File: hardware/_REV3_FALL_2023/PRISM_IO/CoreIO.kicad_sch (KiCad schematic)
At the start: 35 parts, among them J1 Conn_01x04_Socket, J2 COTS_SWITCH_PLUG, J3 PYRO 1, J4 PYRO 2, Q1 AO3400A, Q2 AO3400A, U1 TMC2209_SILENTSTEPSTICK, U2 LD1117S12TR_SOT223

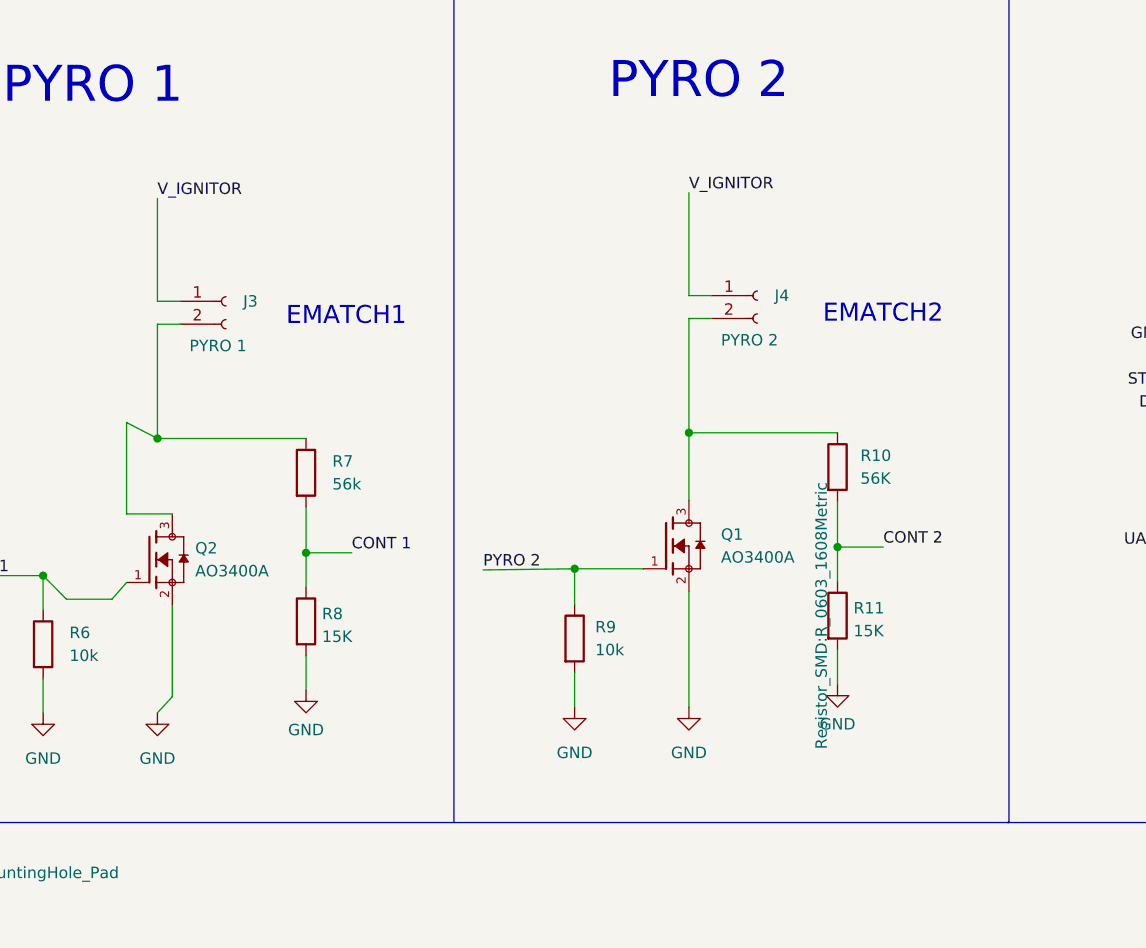
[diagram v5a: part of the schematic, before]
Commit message: add resistors to IO
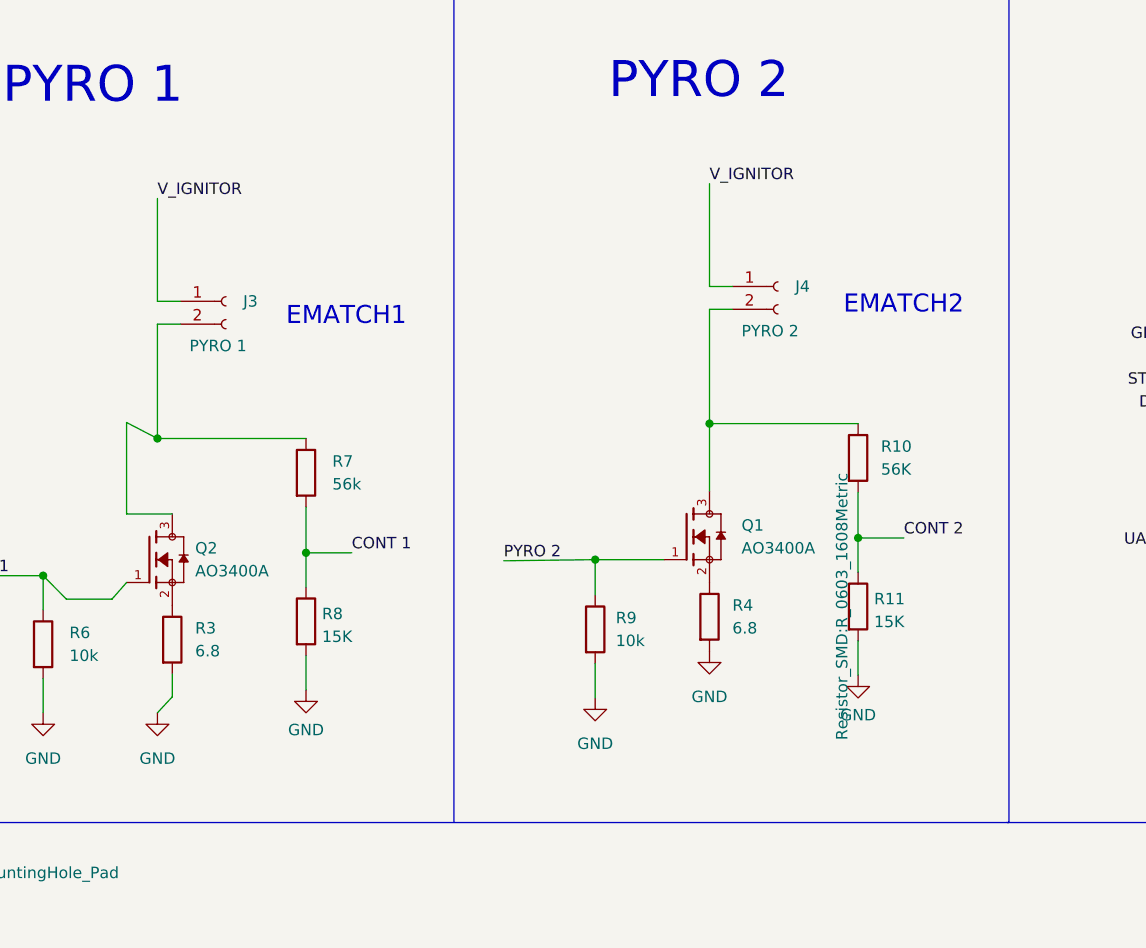
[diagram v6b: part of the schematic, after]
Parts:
- added R3, R4: 6.8, Resistor_THT:R_Axial_DIN0414_L11.9mm_D4.5mm_P15.24mm_Horizontal, symbol Device:R
- C1, C2: footprint Capacitor_SMD:CP_Elec_4x5.4 -> Capacitor_Tantalum_SMD:CP_EIA-3216-18_Kemet-A; Vendor C3001200 -> C7171
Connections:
- net GND: now also R3.2, R4.2; no longer Q1.2, Q2.2
- new net: Q2.2, R3.1
- new net: Q1.2, R4.1
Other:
- moved on the sheet: J4, Q1, R10, R11, R9

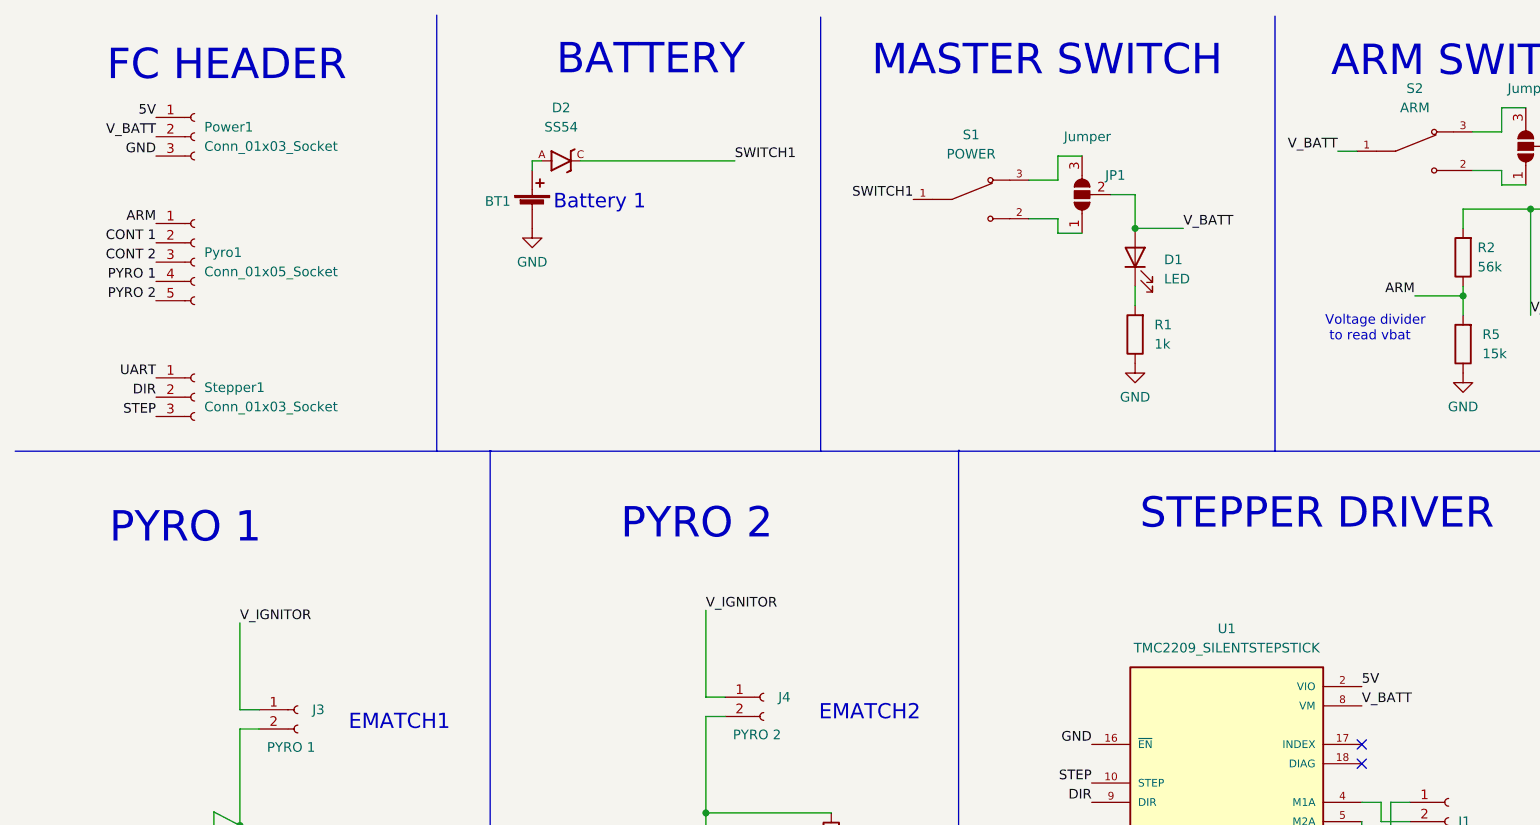
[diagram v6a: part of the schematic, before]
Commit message: Updated Core IO connectors to match updated Teensy board and change stepper to 3.3V
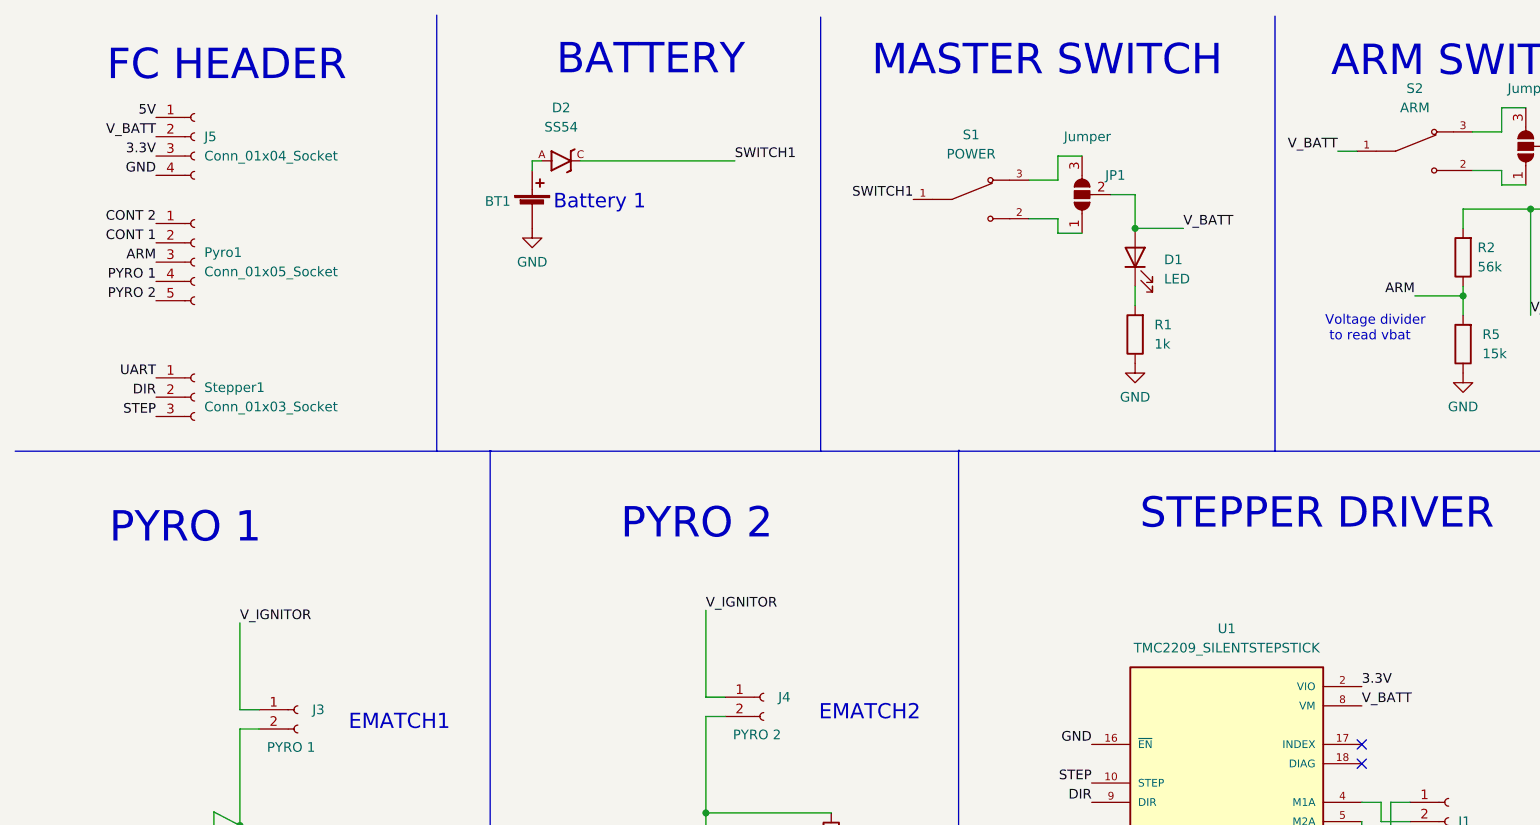
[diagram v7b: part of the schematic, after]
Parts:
- removed Power1: Conn_01x03_Socket, Connector_PinHeader_2.54mm:PinHeader_1x03_P2.54mm_Vertical, symbol Connector:Conn_01x03_Socket
- added J5: Conn_01x04_Socket, Connector_PinHeader_2.54mm:PinHeader_1x04_P2.54mm_Vertical, symbol Connector:Conn_01x04_Socket
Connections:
- net 5V: now also J5.1 (Pin_1); no longer U1.2 (VIO)
- net ARM: now also Pyro1.3 (Pin_3); no longer Pyro1.1 (Pin_1)
- net CONT 2: now also Pyro1.1 (Pin_1); no longer Pyro1.3 (Pin_3)
- net GND: now also J5.4 (Pin_4)
- net V_BATT: now also J5.2 (Pin_2)
- new net 3.3V: J5.3 (Pin_3), U1.2 (VIO)
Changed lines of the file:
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@@
     (effects (font (size 1.27 1.27)) (justify right bottom))
   )
-  (label "ARM" (at 30.48 39.37 180) (fields_autoplaced)
+  (label "ARM" (at 30.48 44.45 180) (fields_autoplaced)
     (effects (font (size 1.27 1.27)) (justify right bottom))
   )
@@
     (effects (font (size 1.27 1.27)) (justify right bottom))
   )
-  (label "5V" (at 189.23 100.33 0) (fields_autoplaced)
+  (label "3.3V" (at 30.48 30.48 180) (fields_autoplaced)
+    (effects (font (size 1.27 1.27)) (justify right bottom))
+  )
+  (label "CONT 2" (at 30.48 39.37 180) (fields_autoplaced)
+    (effects (font (size 1.27 1.27)) (justify right bottom))
+  )
+  (label "PYRO 2" (at 30.48 49.53 180) (fields_autoplaced)
+    (effects (font (size 1.27 1.27)) (justify right bottom))
+  )
+  (label "GND" (at 30.48 33.02 180) (fields_autoplaced)
+    (effects (font (size 1.27 1.27)) (justify right bottom))
+  )
+  (label "V_BATT" (at 186.055 29.845 180) (fields_autoplaced)
+    (effects (font (size 1.27 1.27)) (justify right bottom))
+  )
+  (label "3.3V" (at 189.23 100.33 0) (fields_autoplaced)
     (effects (font (size 1.27 1.27)) (justify left bottom))
-  )
-  (label "CONT 2" (at 30.48 44.45 180) (fields_autoplaced)
-    (effects (font (size 1.27 1.27)) (justify right bottom))
-  )
-  (label "PYRO 2" (at 30.48 49.53 180) (fields_autoplaced)
-    (effects (font (size 1.27 1.27)) (justify right bottom))
-  )
-  (label "GND" (at 30.48 30.48 180) (fields_autoplaced)
-    (effects (font (size 1.27 1.27)) (justify right bottom))
-  )
-  (label "V_BATT" (at 186.055 29.845 180) (fields_autoplaced)
-    (effects (font (size 1.27 1.27)) (justify right bottom))
   )
   (label "UART" (at 153.67 130.81 180) (fields_autoplaced)
@@
         (path "/9e212ca8-0a67-4365-b4eb-6661fcc83758"
           (reference "Q2") (unit 1)
-        )
-      )
-    )
-  )
-  (symbol (lib_id "Connector:Conn_01x03_Socket") (at 35.56 27.94 0) (unit 1)
-    (in_bom yes) (on_board yes) (dnp no) (fields_autoplaced)
-    (property "Reference" "Power1" (at 36.83 26.67 0)
-      (effects (font (size 1.27 1.27)) (justify left))
-    )
-    (property "Value" "Conn_01x03_Socket" (at 36.83 29.21 0)
-      (effects (font (size 1.27 1.27)) (justify left))
-    )
-    (property "Footprint" "Connector_PinHeader_2.54mm:PinHeader_1x03_P2.54mm_Vertical" (at 35.56 27.94 0)
-      (effects (font (size 1.27 1.27)) hide)
-    )
-    (property "Datasheet" "~" (at 35.56 27.94 0)
-      (effects (font (size 1.27 1.27)) hide)
-    )
-    (pin "1")
-    (pin "2")
-    (pin "3")
-    (instances
-      (project "board_one_teensy_22"
-        (path "/7a48c3b0-2761-409e-ae2f-7ebae3820225"
-          (reference "Power1") (unit 1)
-        )
-      )
-      (project "CoreIO"
-        (path "/9e212ca8-0a67-4365-b4eb-6661fcc83758"
-          (reference "Power2") (unit 1)
         )
       )
@@
         )
       )
+    )
+  )
+  (symbol (lib_id "Connector:Conn_01x04_Socket") (at 35.56 27.94 0) (unit 1)
+    (in_bom yes) (on_board yes) (dnp no) (fields_autoplaced)
+    (property "Reference" "J5" (at 36.83 27.94 0)
+      (effects (font (size 1.27 1.27)) (justify left))
+    )
+    (property "Value" "Conn_01x04_Socket" (at 36.83 30.48 0)
+      (effects (font (size 1.27 1.27)) (justify left))
+    )
+    (property "Footprint" "Connector_PinHeader_2.54mm:PinHeader_1x04_P2.54mm_Vertical" (at 35.56 27.94 0)
+      (effects (font (size 1.27 1.27)) hide)
+    )
+    (property "Datasheet" "~" (at 35.56 27.94 0)
+      (effects (font (size 1.27 1.27)) hide)
+    )
+    (pin "3")
+    (pin "4")
+    (pin "1")
+    (pin "2")
+    (instances
+      (project "CoreIO"
+        (path "/9e212ca8-0a67-4365-b4eb-6661fcc83758"
+          (reference "J5") (unit 1)
+        )
+      )
